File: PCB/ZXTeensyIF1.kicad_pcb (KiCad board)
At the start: 2 copper layers, 222.4 x 72.5 mm, 81 parts, among them J1 ESP-01S-Header, J3 Polou D24V5F3, Q1 BC213C, Q10 ZTX313, Q11 ZTX313, Q2 BC213C, Q3 BC184C, Q4 PN2222A, Q5 PN2222A, Q6 BC184C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

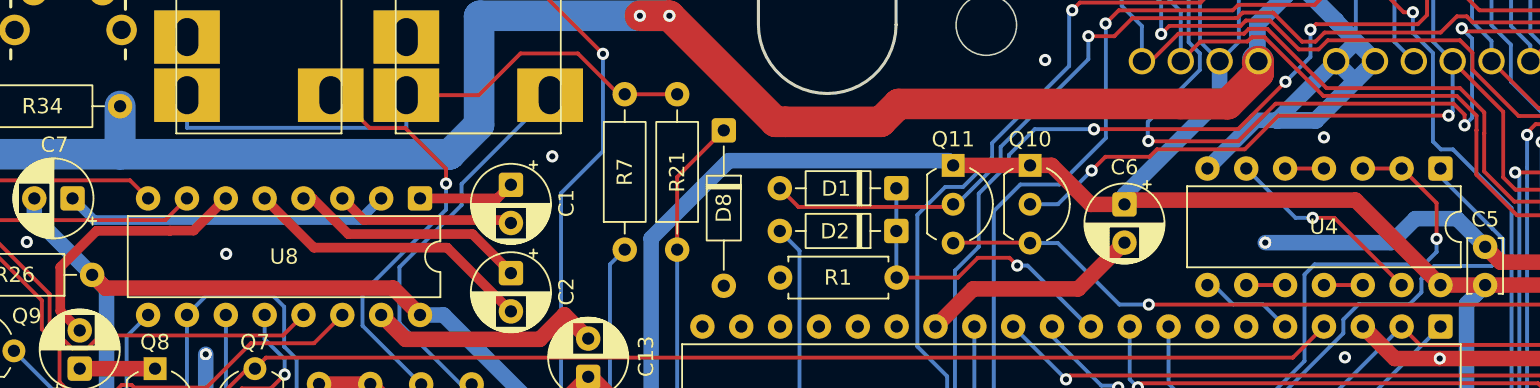
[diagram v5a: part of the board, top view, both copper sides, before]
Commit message: PCB move C6 slightly, C13 to 47uF
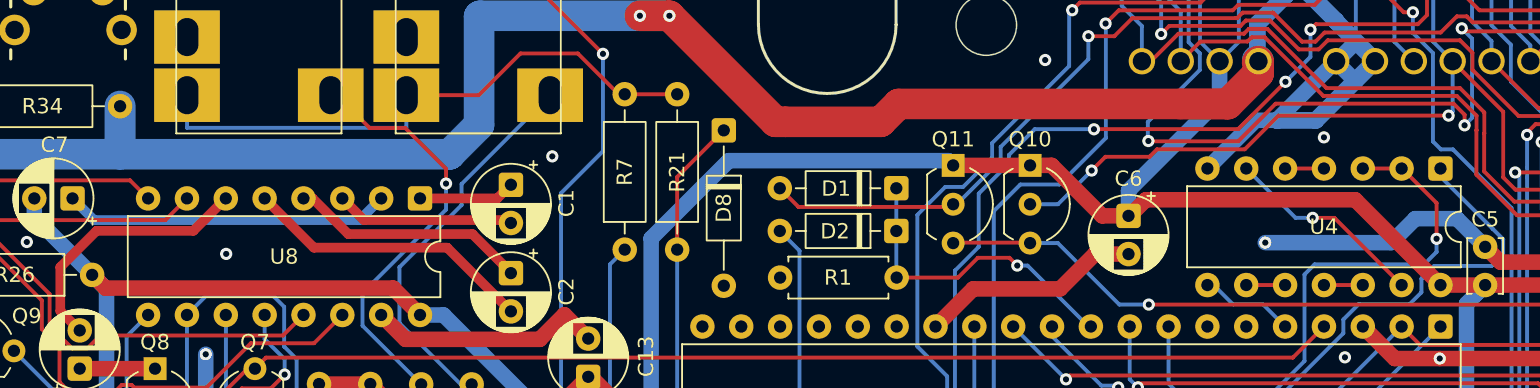
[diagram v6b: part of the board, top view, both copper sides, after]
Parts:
- C13: value 1uF -> 47uF 16V
- moved C6 0.80 mm to (165.2, 84.0)
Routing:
- net +5V: track 273.9 -> 274.7 mm
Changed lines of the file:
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@@
 	(property "PRJ_DATE" "2026-02-23")
 	(property "PRJ_NAME" "ZXTeensyIF1")
-	(property "PRJ_REVISION" "v0.7")
+	(property "PRJ_REVISION" "v0.7b")
 	(net 0 "")
 	(net 1 "+12VAC")
@@
 			)
 		)
-		(property "Value" "1uF"
+		(property "Value" "47uF 16V"
 			(at 1.25 3.75 90)
 			(layer "F.Fab")
@@
 	(footprint "Capacitor_THT:CP_Radial_D5.0mm_P2.50mm"
 		(layer "F.Cu")
-		(at 164.9344 83.2504 -90)
+		(at 165.2 84 -90)
 		(descr "CP, Radial series, Radial, pin pitch=2.50mm, diameter=5mm, height=7mm, Electrolytic Capacitor")
 		(tags "CP Radial series Radial pin pitch 2.50mm diameter 5mm height 7mm Electrolytic Capacitor")
@@
 	)
 	(segment
+		(start 155.0396 88.775)
+		(end 152.5778 91.2368)
+		(width 1.016)
+		(layer "F.Cu")
+		(net 2)
+	)
+	(segment
 		(start 240.9699 90.9828)
 		(end 240.97 90.9827)
@@
 	)
 	(segment
+		(start 165.2 86.5)
+		(end 163 86.5)
+		(width 1.016)
+		(layer "F.Cu")
+		(net 2)
+	)
+	(segment
 		(start 202.1586 85.2732)
 		(end 202.9354 86.05)
@@
 	)
 	(segment
-		(start 161.9094 88.775)
-		(end 155.0396 88.775)
-		(width 1.016)
-		(layer "F.Cu")
-		(net 2)
-	)
-	(segment
 		(start 212.4908 114.0102)
 		(end 212.4908 114.01)
@@
 	)
 	(segment
-		(start 155.0396 88.775)
-		(end 152.5778 91.2368)
-		(width 1.016)
-		(layer "F.Cu")
-		(net 2)
-	)
-	(segment
 		(start 47.3234 99.5073)
 		(end 47.3587 99.5426)
@@
 	)
 	(segment
-		(start 164.934 85.7504)
-		(end 161.9094 88.775)
+		(start 104 101.4122)
+		(end 104 100.814)
 		(width 1.016)
 		(layer "F.Cu")
@@
 	)
 	(segment
-		(start 104 101.4122)
-		(end 104 100.814)
+		(start 205.0119 86.0619)
+		(end 205.0119 87.8282)
 		(width 1.016)
 		(layer "F.Cu")
@@
 	)
 	(segment
-		(start 205.0119 86.0619)
-		(end 205.0119 87.8282)
+		(start 163 86.5)
+		(end 160.725 88.775)
 		(width 1.016)
 		(layer "F.Cu")
@@
 	)
 	(segment
+		(start 160.725 88.775)
+		(end 155.0396 88.775)
+		(width 1.016)
+		(layer "F.Cu")
+		(net 2)
+	)
+	(segment
 		(start 231.84 86.34)
 		(end 233.39 86.34)
@@
 	)
 	(segment
-		(start 180.0426 82.9692)
-		(end 185.5978 88.5244)
+		(start 165.275 84)
+		(end 165.2 84)
 		(width 1.016)
 		(layer "F.Cu")
@@
 	)
 	(segment
-		(start 164.9344 83.2504)
-		(end 162.727 83.2504)
-		(width 1.016)
-		(layer "F.Cu")
-		(net 5)
-	)
-	(segment
-		(start 162.727 83.2504)
-		(end 160.1724 80.6958)
+		(start 188.5188 88.5244)
+		(end 188.519 88.5244)
 		(width 1.016)
 		(layer "F.Cu")
@@
 	)
 	(segment
-		(start 188.5188 88.5244)
-		(end 188.519 88.5244)
+		(start 98.298 88.7222)
+		(end 97.4344 87.8586)
 		(width 1.016)
 		(layer "F.Cu")
@@
 	)
 	(segment
-		(start 98.298 88.7222)
-		(end 97.4344 87.8586)
+		(start 163.4766 84)
+		(end 160.1724 80.6958)
 		(width 1.016)
 		(layer "F.Cu")
@@
 	)
 	(segment
+		(start 118.2724 97.6476)
+		(end 115.6208 94.996)
+		(width 1.016)
+		(layer "F.Cu")
+		(net 5)
+	)
+	(segment
+		(start 153.733 80.7004)
+		(end 158.7622 80.7004)
+		(width 1.016)
+		(layer "F.Cu")
+		(net 5)
+	)
+	(segment
 		(start 160.1724 80.6958)
 		(end 158.7668 80.6958)
@@
 	)
 	(segment
-		(start 118.2724 97.6476)
-		(end 115.6208 94.996)
+		(start 200.167 88.5244)
+		(end 200.863 87.8282)
 		(width 1.016)
 		(layer "F.Cu")
@@
 	)
 	(segment
-		(start 153.733 80.7004)
+		(start 158.7668 80.6958)
 		(end 158.7622 80.7004)
 		(width 1.016)
@@
 	)
 	(segment
-		(start 200.167 88.5244)
-		(end 200.863 87.8282)
+		(start 185.5978 88.5244)
+		(end 180.0234 82.95)
 		(width 1.016)
 		(layer "F.Cu")
@@
 	)
 	(segment
-		(start 164.9344 83.2504)
-		(end 165.2156 82.9692)
+		(start 166.325 82.95)
+		(end 165.275 84)
 		(width 1.016)
 		(layer "F.Cu")
@@
 	)
 	(segment
-		(start 165.2156 82.9692)
-		(end 180.0426 82.9692)
+		(start 180.0234 82.95)
+		(end 166.325 82.95)
 		(width 1.016)
 		(layer "F.Cu")
@@
 	)
 	(segment
-		(start 112.268 94.996)
-		(end 115.6208 94.996)
+		(start 165.2 84)
+		(end 163.4766 84)
 		(width 1.016)
 		(layer "F.Cu")
@@
 	)
 	(segment
-		(start 118.872 90.4798)
-		(end 117.1144 88.7222)
+		(start 112.268 94.996)
+		(end 115.6208 94.996)
 		(width 1.016)
 		(layer "F.Cu")
@@
 	)
 	(segment
-		(start 158.7668 80.6958)
-		(end 158.7622 80.7004)
+		(start 118.872 90.4798)
+		(end 117.1144 88.7222)
 		(width 1.016)
 		(layer "F.Cu")
@@
 	)
 	(segment
-		(start 164.934 82.6144)
-		(end 171.155 76.3934)
-		(width 1.016)
-		(layer "B.Cu")
-		(net 5)
-	)
-	(segment
 		(start 171.1547 73.8886)
 		(end 171.155 73.8886)
@@
 	)
 	(segment
+		(start 165.2 82.3484)
+		(end 171.155 76.3934)
+		(width 1.016)
+		(layer "B.Cu")
+		(net 5)
+	)
+	(segment
 		(start 153.4236 80.391)
 		(end 139.065 80.391)
@@
 	)
 	(segment
-		(start 164.934 83.2504)
-		(end 164.934 82.7864)
+		(start 171.155 76.3934)
+		(end 171.155 73.8886)
 		(width 1.016)
 		(layer "B.Cu")
@@
 	)
 	(segment
-		(start 164.934 82.7864)
-		(end 164.934 82.6144)
-		(width 1.016)
-		(layer "B.Cu")
-		(net 5)
-	)
-	(segment
 		(start 169.875 67.7416)
 		(end 169.875 72.6089)
@@
 	)
 	(segment
-		(start 164.934 82.7864)
-		(end 164.934 83.25)
+		(start 165.2 84)
+		(end 165.2 82.3484)
 		(width 1.016)
 		(layer "B.Cu")
@@
 	)
 	(segment
-		(start 171.155 76.3934)
-		(end 171.155 73.8886)
-		(width 1.016)
-		(layer "B.Cu")
-		(net 5)
-	)
-	(segment
 		(start 187.9095 89.134)
 		(end 188.5188 88.5247)
@@
 	)
 	(segment
-		(start 164.934 83.25)
-		(end 164.9344 83.2504)
-		(width 1.016)
-		(layer "B.Cu")
-		(net 5)
-	)
-	(segment
 		(start 118.872 90.4798)
 		(end 120.4092 90.4798)
@@
 	)
 	(segment
-		(start 102.504342 84.9767)
+		(start 104.0551 84.9767)
 		(end 97.7255 84.9767)
 		(width 0.635)
@@
 	)
 	(segment
-		(start 104.0688 84.963)
-		(end 102.518042 84.963)
+		(start 95.3516 90.2208)
+		(end 96.6216 91.4908)
 		(width 0.635)
 		(layer "F.Cu")
@@
 	(segment
 		(start 106.172 82.8598)
-		(end 104.0688 84.963)
-		(width 0.635)
-		(layer "F.Cu")
-		(net 159)
-	)
-	(segment
-		(start 95.3516 87.3506)
-		(end 95.3516 90.2208)
+		(end 104.0551 84.9767)
 		(width 0.635)
 		(layer "F.Cu")
@@
 	)
 	(segment
-		(start 95.3516 90.2208)
-		(end 96.6216 91.4908)
-		(width 0.635)
-		(layer "F.Cu")
-		(net 159)
-	)
-	(segment
-		(start 102.518042 84.963)
-		(end 102.504342 84.9767)
+		(start 95.3516 87.3506)
+		(end 95.3516 90.2208)
 		(width 0.635)
 		(layer "F.Cu")
